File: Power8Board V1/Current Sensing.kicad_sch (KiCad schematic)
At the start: 10 parts, among them U12 ADS1015IDGS, U13 ADS1015IDGS

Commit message: Beginning to layout.
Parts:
- removed FB3, FB4: FerriteBead, symbol Device:FerriteBead
- C20, C22: footprint (none) -> Capacitor_SMD:C_0805_2012Metric; Mfr. (none) -> Murata Electronics; Order Link (none) -> https://www.digikey.com/en/products/detail/murata-electroni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; Part # (none) -> GRT21BC71E106KE13L; Price (none) -> $0.32
- C21, C23: footprint (none) -> Capacitor_SMD:C_0805_2012Metric; Mfr. (none) -> KEMET; Order Link (none) -> https://www.digikey.com/en/products/detail/kemet/C0805C104J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; Part # (none) -> C0805C104J5RACAUTO; Price (none) -> $0.109
- FB1, FB2: footprint (none) -> MPZ2012S102ATD25:BEADC2012X105N; Mfr. (none) -> TDK Corporation; Order Link (none) -> https://www.digikey.com/en/products/detail/tdk-corporation/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; Part # (none) -> MPZ2012S102ATD25; Price (none) -> $0.084
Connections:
- net GNDA/2 is gone; now on net GND: C23.2, U13.3 (GND)
- net +3.3VA/2: now also FB2.2
- net 3.3V: now also FB2.1
- net GND: now also C21.2, U12.3 (GND); no longer FB2.1
- removed net GNDA/1: C21.2, FB2.2, U12.3 (GND)

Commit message: Laid out components
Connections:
- net +3.3VA/2: now also U13.1 (ADDR)
- net 3.3V: no longer U13.1 (ADDR)
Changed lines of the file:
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@@
-		)
-	)
-	(hierarchical_label "3.3V"
-		(shape input)
-		(at 227.965 99.06 0)
-		(fields_autoplaced yes)
-		(effects
-			(font
-				(size 1.27 1.27)
-			)
-			(justify left)
 		)
 	)
@@
 					(unit 1)
 				)
+			)
+		)
+	)
+	(symbol
+		(lib_id "power:+3.3VA")
+		(at 227.965 99.06 270)
+		(unit 1)
+		(exclude_from_sim no)
+		(in_bom yes)
+		(on_board yes)
+		(dnp no)
+		(property "Reference" "#PWR030"
+			(at 224.155 99.06 0)
+			(effects
+				(font
+					(size 1.27 1.27)
+				)
+				(hide yes)
+			)
+		)
+		(property "Value" "+3.3VA/2"
+			(at 236.22 99.06 90)
+			(effects
+				(font
+					(size 1.27 1.27)
+				)
+			)
+		)
+		(property "Footprint" ""
+			(at 227.965 99.06 0)
+			(effects
+				(font
+					(size 1.27 1.27)
+				)
+				(hide yes)
+			)
+		)
+		(property "Datasheet" ""
+			(at 227.965 99.06 0)
+			(effects
+				(font
+					(size 1.27 1.27)
+				)
+				(hide yes)
+			)
+		)
+		(property "Description" "Power symbol creates a global label with name \"+3.3VA\""
+			(at 227.965 99.06 0)
+			(effects
+				(font
+					(size 1.27 1.27)
+				)
+				(hide yes)
+			)
+		)
+		(pin "1"
+		)
+		(instances
+			(project "Power8Board V1"
+				(path "/835b92cb-5206-4b93-b4be-2a785f4797f4/64832d79-2054-4fdb-82f6-de66896e6610"
+					(reference "#PWR030")
+					(unit 1)
+				)

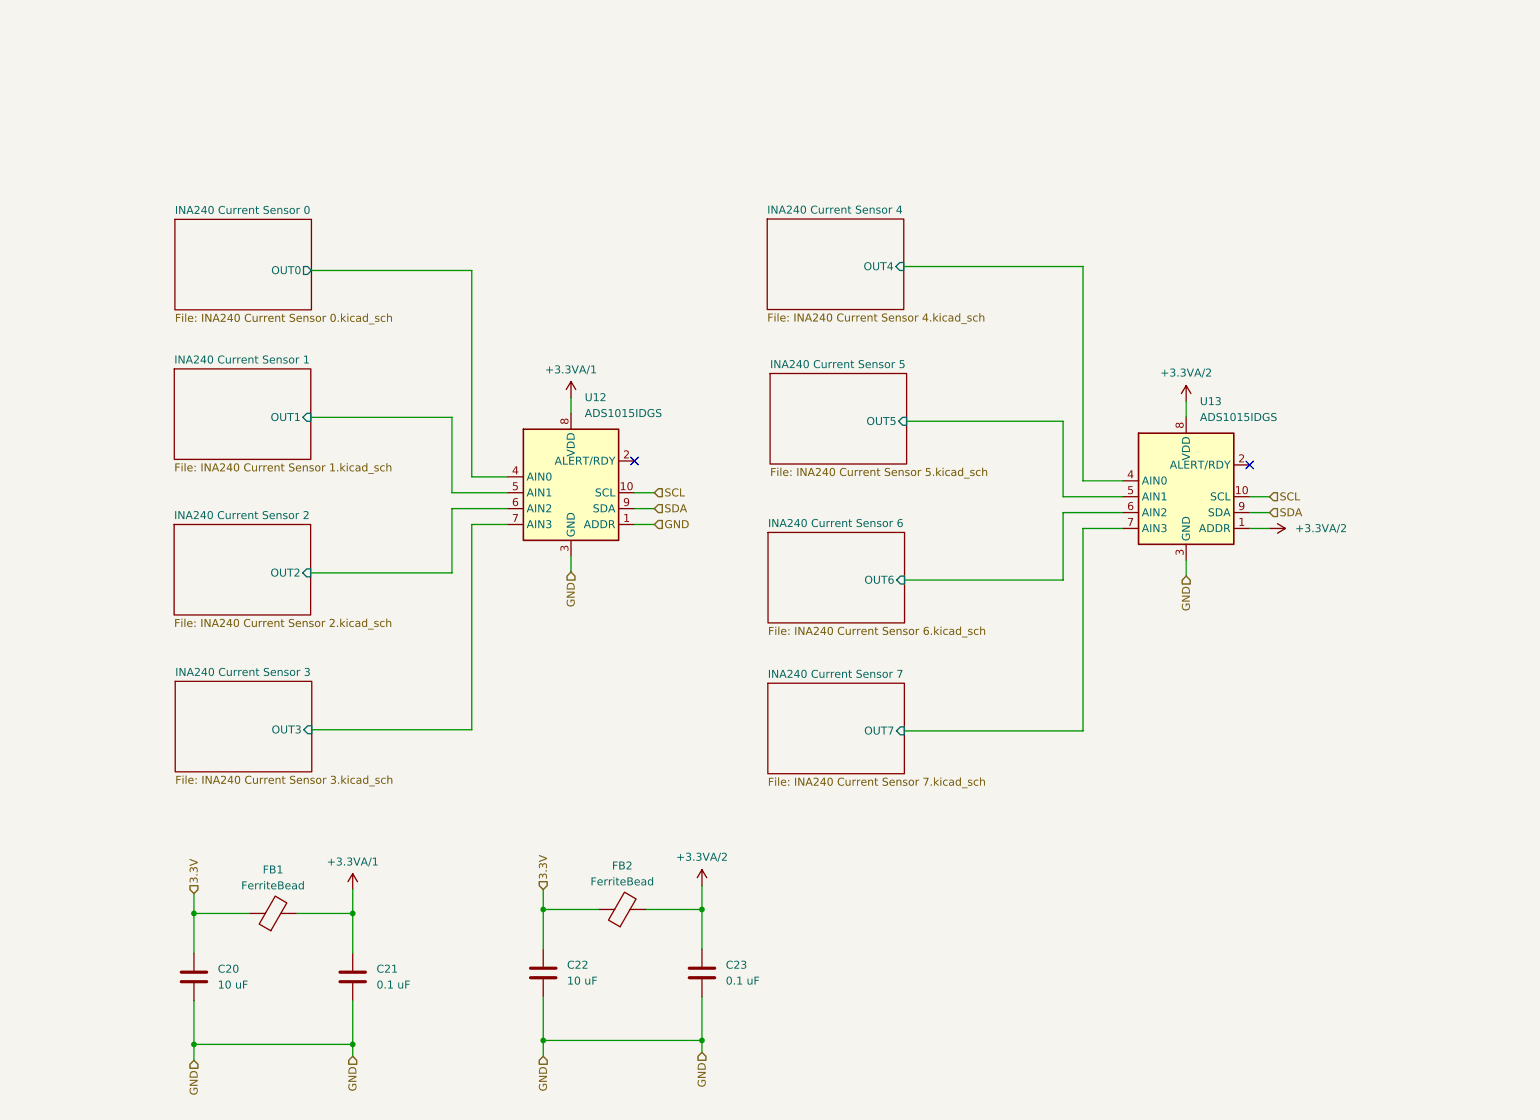
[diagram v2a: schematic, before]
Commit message: Added 0603 components and RC filters.
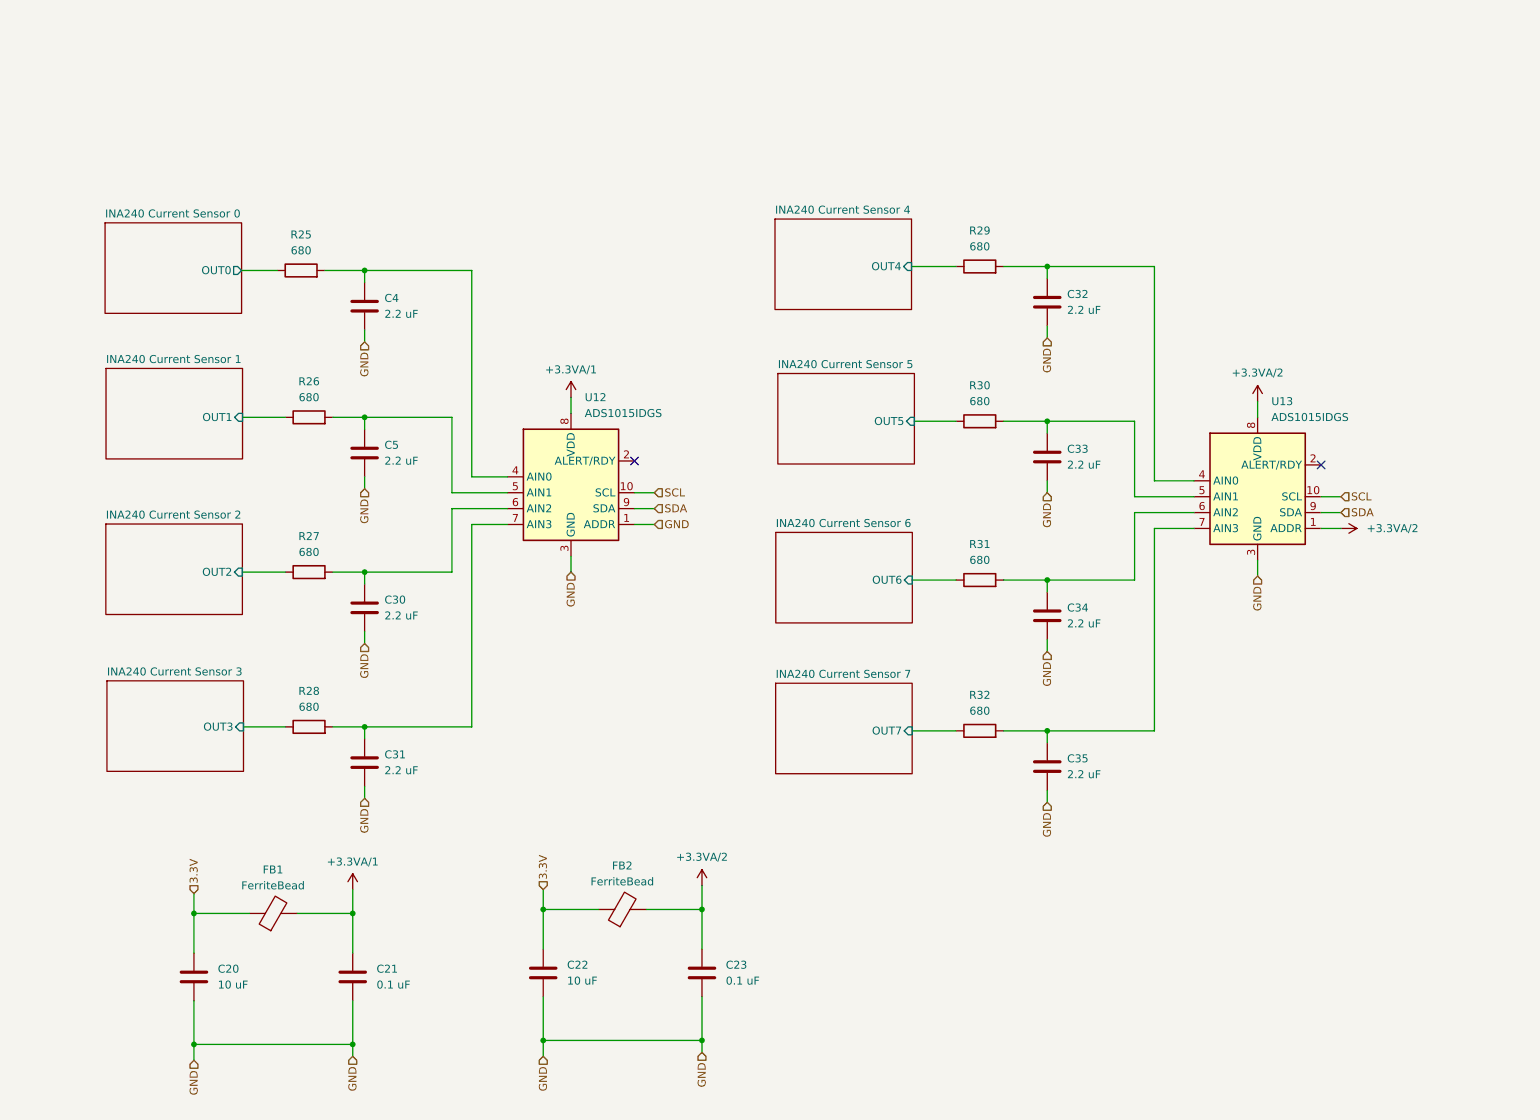
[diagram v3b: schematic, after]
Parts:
- added C30, C31, C32, C33, C34, C35, C4, C5: 2.2 uF, Capacitor_SMD:C_0603_1608Metric, symbol Device:C
- added R25, R26, R27, R28, R29, R30, R31, R32: 680, Resistor_SMD:R_0603_1608Metric, symbol Device:R
- C20, C22: footprint Capacitor_SMD:C_0805_2012Metric -> Capacitor_SMD:C_0603_1608Metric; Order Link https://www.digikey.com/en/products/detail/murata-electronics/GRT21BC71E106KE13L/10697404 -> https://www.digikey.com/en/products/detail/murata-electronics/GRM188R61E106KA73D/9867922; Part # GRT21BC71E106KE13L -> GRM188R61E106KA73D; Price $0.32 -> $0.135
- C21: footprint Capacitor_SMD:C_0805_2012Metric -> Capacitor_SMD:C_0603_1608Metric; Order Link https://www.digikey.com/en/products/detail/kemet/C0805C104J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 -> https://www.digikey.com/en/products/detail/kemet/C0603C104K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; Part # C0805C104J5RACAUTO -> C0603C104K5RACTU; Price $0.109 -> $0.011
- FB1, FB2: footprint MPZ2012S102ATD25:BEADC2012X105N -> 0603 Ferrite Bead:0603 Ferrite Bead; Mfr. TDK Corporation -> Murata Electronics; Order Link https://www.digikey.com/en/products/detail/tdk-corporation/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 -> https://www.digikey.com/en/products/detail/murata-electroni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; Part # MPZ2012S102ATD25 -> BLM18KG102SZ1D; Price $0.084 -> $0.046
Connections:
- net GND: now also C30.2, C31.2, C32.2, C33.2, C34.2, C35.2, C4.2, C5.2
- net INA240 Current Sensor 0/OUT0: now also R25.1; no longer U12.4 (AIN0)
- net INA240 Current Sensor 1/OUT1: now also R26.1; no longer U12.5 (AIN1)
- net INA240 Current Sensor 2/OUT2: now also R27.1; no longer U12.6 (AIN2)
- net INA240 Current Sensor 3/OUT3: now also R28.1; no longer U12.7 (AIN3)
- net INA240 Current Sensor 4/OUT4: now also R29.1; no longer U13.4 (AIN0)
- net INA240 Current Sensor 5/OUT5: now also R30.1; no longer U13.5 (AIN1)
- net INA240 Current Sensor 6/OUT6: now also R31.1; no longer U13.6 (AIN2)
- net INA240 Current Sensor 7/OUT7: now also R32.1; no longer U13.7 (AIN3)
- new net: C4.1, R25.2, U12.4 (AIN0)
- new net: C31.1, R28.2, U12.7 (AIN3)
- new net: C34.1, R31.2, U13.6 (AIN2)
- new net: C33.1, R30.2, U13.5 (AIN1)
- new net: C32.1, R29.2, U13.4 (AIN0)
- new net: C30.1, R27.2, U12.6 (AIN2)
- new net: C35.1, R32.2, U13.7 (AIN3)
- new net: C5.1, R26.2, U12.5 (AIN1)
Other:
- moved on the sheet: U13

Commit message: 9/22 Progress
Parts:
- C23: footprint Capacitor_SMD:C_0805_2012Metric -> Capacitor_SMD:C_0603_1608Metric; Order Link https://www.digikey.com/en/products/detail/kemet/C0805C104J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 -> https://www.digikey.com/en/products/detail/kemet/C0603C104K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; Part # C0805C104J5RACAUTO -> C0603C104K5RACTU; Price $0.109 -> $0.011
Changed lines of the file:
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@@
+	)
+	(symbol
+		(lib_id "Device:R")
+		(at 74.295 130.81 90)
+		(unit 1)
+		(exclude_from_sim no)
+		(in_bom yes)
+		(on_board yes)
+		(dnp no)
+		(fields_autoplaced yes)
+		(property "Reference" "R28"
+			(at 74.295 125.095 90)
+			(effects
+				(font
+					(size 1.27 1.27)
+				)
+			)
+		)
+		(property "Value" "680"
+			(at 74.295 127.635 90)
+			(effects
+				(font
+					(size 1.27 1.27)
+				)
+			)
+		)
+		(property "Footprint" "Resistor_SMD:R_0603_1608Metric"
+			(at 74.295 132.588 90)
+			(effects
+				(font
+					(size 1.27 1.27)
+				)
+				(hide yes)
+			)
+		)
+		(property "Datasheet" "https://www.te.com/commerce/DocumentDelivery/DDEController?Action=srchrtrv&DocNm=1773204-3&DocType=Data%20Sheet&DocLang=English&DocFormat=pdf&PartCntxt=4-2176338-3"
+			(at 74.295 130.81 0)
+			(effects
+				(font
+					(size 1.27 1.27)
+				)
+				(hide yes)
+			)
+		)
+		(property "Description" "RES 680 OHM 1% 1/10W 0603"
+			(at 74.295 130.81 0)
+			(effects
+				(font
+					(size 1.27 1.27)
+				)
+				(hide yes)
+			)
+		)
+		(property "Mfr." "TE Connectivity Passive Product"
+			(at 74.295 130.81 90)
+			(effects
+				(font
+					(size 1.27 1.27)
+				)
+				(hide yes)
+			)
+		)
+		(property "Part #" "CRGCQ0603F680R"
+			(at 74.295 130.81 90)
+			(effects
+				(font
+					(size 1.27 1.27)
+				)
+				(hide yes)
+			)
+		)
+		(property "Price" "$0.028"
+			(at 74.295 130.81 90)
+			(effects
+				(font
+					(size 1.27 1.27)
+				)
+				(hide yes)
+			)
+		)
+		(property "Order Link" "https://www.digikey.com/en/products/detail/te-connectivity-passive-product/CRGCQ0603F680R/8576288?s=N4IgjCBcoEwAwA4CsVQGMoDMCGAbAzgKYA0IA9lANogBsCcABAPIAWAtviALqkAOALlBABVAHYBLfk0wBZQtnwBXAE6EQAX3WkYVEAGEASgHE9ARTg04AZgBi3dUA"
+			(at 74.295 130.81 90)
+			(effects
+				(font
+					(size 1.27 1.27)
+				)
+				(hide yes)
+			)
+		)
+		(pin "2"
+		)
+		(pin "1"
+		)
+		(instances
+			(project "Power8Board V1"
+				(path "/835b92cb-5206-4b93-b4be-2a785f4797f4/64832d79-2054-4fdb-82f6-de66896e6610"
+					(reference "R28")
+					(unit 1)
+				)
+			)
+		)
 	)
 	(symbol
@@
 			)
 		)
-		(property "Footprint" "Capacitor_SMD:C_0805_2012Metric"
+		(property "Footprint" "Capacitor_SMD:C_0603_1608Metric"
 			(at 138.1252 173.99 0)
 			(effects
@@
 			)
 		)
-		(property "Datasheet" "https://content.kemet.com/datasheets/KEM_C1023_X7R_AUTO_SMD.pdf"
-			(at 137.16 170.18 0)
-			(effects
-				(font
-					(size 1.27 1.27)
-				)
-				(hide yes)
-			)
-		)
-		(property "Description" "0.1 uF 0805 Ceramic Capacitor - Automotive, Bypass, Decoupling"
+		(property "Datasheet" "https://www.yageogroup.com/content/datasheet/asset/file/KEM_C1002_X7R_SMD"
+			(at 137.16 170.18 0)
+			(effects
+				(font
+					(size 1.27 1.27)
+				)
+				(hide yes)
+			)
+		)
+		(property "Description" "CAP CER 0.1UF 50V X7R 0603"
 			(at 137.16 170.18 0)
 			(effects
@@
 			)
 		)
-		(property "Part #" "C0805C104J5RACAUTO"
-			(at 137.16 170.18 0)
-			(effects
-				(font
-					(size 1.27 1.27)
-				)
-				(hide yes)
-			)
-		)
-		(property "Price" "$0.109"
-			(at 137.16 170.18 0)
-			(effects
-				(font
-					(size 1.27 1.27)
-				)
-				(hide yes)
-			)
-		)
-		(property "Order Link" "https://www.digikey.com/en/products/detail/kemet/C0805C104J5RACAUTO/3314919"
+		(property "Part #" "C0603C104K5RACTU"
+			(at 137.16 170.18 0)
+			(effects
+				(font
+					(size 1.27 1.27)
+				)
+				(hide yes)
+			)
+		)
+		(property "Price" "$0.011"
+			(at 137.16 170.18 0)
+			(effects
+				(font
+					(size 1.27 1.27)
+				)
+				(hide yes)
+			)
+		)
+		(property "Order Link" "https://www.digikey.com/en/products/detail/kemet/C0603C104K5RACTU/1465594"
 			(at 137.16 170.18 0)
 			(effects
@@
 					(unit 1)
 				)
-			)
-		)
-	)
-	(symbol
-		(lib_id "Device:R")
-		(at 74.295 130.81 90)
-		(unit 1)
-		(exclude_from_sim no)
-		(in_bom yes)
-		(on_board yes)
-		(dnp no)
-		(fields_autoplaced yes)
-		(property "Reference" "R28"
-			(at 74.295 125.095 90)
-			(effects
-				(font
-					(size 1.27 1.27)
-				)
-			)
-		)
-		(property "Value" "680"
-			(at 74.295 127.635 90)
-			(effects
-				(font
-					(size 1.27 1.27)
-				)
-			)
-		)
-		(property "Footprint" "Resistor_SMD:R_0603_1608Metric"
-			(at 74.295 132.588 90)
-			(effects
-				(font
-					(size 1.27 1.27)
-				)
-				(hide yes)
-			)
-		)
-		(property "Datasheet" "https://www.te.com/commerce/DocumentDelivery/DDEController?Action=srchrtrv&DocNm=1773204-3&DocType=Data%20Sheet&DocLang=English&DocFormat=pdf&PartCntxt=4-2176338-3"
-			(at 74.295 130.81 0)
-			(effects
-				(font
-					(size 1.27 1.27)
-				)
-				(hide yes)
-			)
-		)
-		(property "Description" "RES 680 OHM 1% 1/10W 0603"
-			(at 74.295 130.81 0)
-			(effects
-				(font
-					(size 1.27 1.27)
-				)
-				(hide yes)
-			)
-		)
-		(property "Mfr." "TE Connectivity Passive Product"
-			(at 74.295 130.81 90)
-			(effects
-				(font
-					(size 1.27 1.27)
-				)
-				(hide yes)
-			)
-		)
-		(property "Part #" "CRGCQ0603F680R"
-			(at 74.295 130.81 90)
-			(effects
-				(font
-					(size 1.27 1.27)
-				)
-				(hide yes)
-			)
-		)
-		(property "Price" "$0.028"
-			(at 74.295 130.81 90)
-			(effects
-				(font
-					(size 1.27 1.27)
-				)
-				(hide yes)
-			)
-		)
-		(property "Order Link" "https://www.digikey.com/en/products/detail/te-connectivity-passive-product/CRGCQ0603F680R/8576288?s=N4IgjCBcoEwAwA4CsVQGMoDMCGAbAzgKYA0IA9lANogBsCcABAPIAWAtviALqkAOALlBABVAHYBLfk0wBZQtnwBXAE6EQAX3WkYVEAGEASgHE9ARTg04AZgBi3dUA"
-			(at 74.295 130.81 90)
-			(effects
-				(font
-					(size 1.27 1.27)
-				)
-				(hide yes)
-			)
-		)
-		(pin "2"
-		)
-		(pin "1"
-		)
-		(instances
-			(project "Power8Board V1"
-				(path "/835b92cb-5206-4b93-b4be-2a785f4797f4/64832d79-2054-4fdb-82f6-de66896e6610"
-					(reference "R28")
-					(unit 1)
-				)

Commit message: DRC sorted out.
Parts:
- removed R25: 680, Resistor_SMD:R_0603_1608Metric, symbol Device:R
- added R5: 680, Resistor_SMD:R_0603_1608Metric, symbol Device:R
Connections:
- net INA240 Current Sensor 0/OUT0: now also R5.1
- net at C4.1, U12.4 (AIN0): now also R5.2
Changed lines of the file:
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@@
+	(symbol
+		(lib_id "Device:R")
+		(at 73.025 57.785 90)
+		(unit 1)
+		(exclude_from_sim no)
+		(in_bom yes)
+		(on_board yes)
+		(dnp no)
+		(fields_autoplaced yes)
+		(property "Reference" "R5"
+			(at 73.025 52.07 90)
+			(effects
+				(font
+					(size 1.27 1.27)
+				)
+			)
+		)
+		(property "Value" "680"
+			(at 73.025 54.61 90)
+			(effects
+				(font
+					(size 1.27 1.27)
+				)
+			)
+		)
+		(property "Footprint" "Resistor_SMD:R_0603_1608Metric"
+			(at 73.025 59.563 90)
+			(effects
+				(font
+					(size 1.27 1.27)
+				)
+				(hide yes)
+			)
+		)
+		(property "Datasheet" "https://www.te.com/commerce/DocumentDelivery/DDEController?Action=srchrtrv&DocNm=1773204-3&DocType=Data%20Sheet&DocLang=English&DocFormat=pdf&PartCntxt=4-2176338-3"
+			(at 73.025 57.785 0)
+			(effects
+				(font
+					(size 1.27 1.27)
+				)
+				(hide yes)
+			)
+		)
+		(property "Description" "RES 680 OHM 1% 1/10W 0603"
+			(at 73.025 57.785 0)
+			(effects
+				(font
+					(size 1.27 1.27)
+				)
+				(hide yes)
+			)
+		)
+		(property "Mfr." "TE Connectivity Passive Product"
+			(at 73.025 57.785 90)
+			(effects
+				(font
+					(size 1.27 1.27)
+				)
+				(hide yes)
+			)
+		)
+		(property "Part #" "CRGCQ0603F680R"
+			(at 73.025 57.785 90)
+			(effects
+				(font
+					(size 1.27 1.27)
+				)
+				(hide yes)
+			)
+		)
+		(property "Price" "$0.028"
+			(at 73.025 57.785 90)
+			(effects
+				(font
+					(size 1.27 1.27)
+				)
+				(hide yes)
+			)
+		)
+		(property "Order Link" "https://www.digikey.com/en/products/detail/te-connectivity-passive-product/CRGCQ0603F680R/8576288?s=N4IgjCBcoEwAwA4CsVQGMoDMCGAbAzgKYA0IA9lANogBsCcABAPIAWAtviALqkAOALlBABVAHYBLfk0wBZQtnwBXAE6EQAX3WkYVEAGEASgHE9ARTg04AZgBi3dUA"
+			(at 73.025 57.785 90)
+			(effects
+				(font
+					(size 1.27 1.27)
+				)
+				(hide yes)
+			)
+		)
+		(pin "2"
+		)
+		(pin "1"
+		)
+		(instances
+			(project "Power8Board V1"
+				(path "/835b92cb-5206-4b93-b4be-2a785f4797f4/64832d79-2054-4fdb-82f6-de66896e6610"
+					(reference "R5")
+					(unit 1)
+				)
+			)
+		)
+	)
 	(symbol
 		(lib_id "Device:R")
@@
 					(unit 1)
 				)
-			)
-		)
-	)
-	(symbol
-		(lib_id "Device:R")
-		(at 73.025 57.785 90)
-		(unit 1)
-		(exclude_from_sim no)
-		(in_bom yes)
-		(on_board yes)
-		(dnp no)
-		(fields_autoplaced yes)
-		(property "Reference" "R25"
-			(at 73.025 52.07 90)
-			(effects
-				(font
-					(size 1.27 1.27)
-				)
-			)
-		)
-		(property "Value" "680"
-			(at 73.025 54.61 90)
-			(effects
-				(font
-					(size 1.27 1.27)
-				)
-			)
-		)
-		(property "Footprint" "Resistor_SMD:R_0603_1608Metric"
-			(at 73.025 59.563 90)
-			(effects
-				(font
-					(size 1.27 1.27)
-				)
-				(hide yes)
-			)
-		)
-		(property "Datasheet" "https://www.te.com/commerce/DocumentDelivery/DDEController?Action=srchrtrv&DocNm=1773204-3&DocType=Data%20Sheet&DocLang=English&DocFormat=pdf&PartCntxt=4-2176338-3"
-			(at 73.025 57.785 0)
-			(effects
-				(font
-					(size 1.27 1.27)
-				)
-				(hide yes)
-			)
-		)
-		(property "Description" "RES 680 OHM 1% 1/10W 0603"
-			(at 73.025 57.785 0)
-			(effects
-				(font
-					(size 1.27 1.27)
-				)
-				(hide yes)
-			)
-		)
-		(property "Mfr." "TE Connectivity Passive Product"
-			(at 73.025 57.785 90)
-			(effects
-				(font
-					(size 1.27 1.27)
-				)
-				(hide yes)
-			)
-		)
-		(property "Part #" "CRGCQ0603F680R"
-			(at 73.025 57.785 90)
-			(effects
-				(font
-					(size 1.27 1.27)
-				)
-				(hide yes)
-			)
-		)
-		(property "Price" "$0.028"
-			(at 73.025 57.785 90)
-			(effects
-				(font
-					(size 1.27 1.27)
-				)
-				(hide yes)
-			)
-		)
-		(property "Order Link" "https://www.digikey.com/en/products/detail/te-connectivity-passive-product/CRGCQ0603F680R/8576288?s=N4IgjCBcoEwAwA4CsVQGMoDMCGAbAzgKYA0IA9lANogBsCcABAPIAWAtviALqkAOALlBABVAHYBLfk0wBZQtnwBXAE6EQAX3WkYVEAGEASgHE9ARTg04AZgBi3dUA"
-			(at 73.025 57.785 90)
-			(effects
-				(font
-					(size 1.27 1.27)
-				)
-				(hide yes)
-			)
-		)
-		(pin "2"
-		)
-		(pin "1"
-		)
-		(instances
-			(project ""
-				(path "/835b92cb-5206-4b93-b4be-2a785f4797f4/64832d79-2054-4fdb-82f6-de66896e6610"
-					(reference "R25")
-					(unit 1)
-				)
